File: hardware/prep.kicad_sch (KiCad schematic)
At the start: 20 parts, among them U1 LD1117S33TR_SOT223, U2 LM4040DBZ-10

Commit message: Corrected resistor package, deleted unused files and gerbers
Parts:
- FB1, FB2, FB3, FB4: LCSC (none) -> C73326
- R1: footprint Resistor_SMD:R_4020_10251Metric -> Resistor_SMD:R_0402_1005Metric
- U1: LCSC (none) -> C86781
- U2: LCSC (none) -> C3717582
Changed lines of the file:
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@@
+			)
+		)
+		(property "LCSC" "C3717582"
+			(at 198.12 119.38 0)
+			(effects
+				(font
+					(size 1.27 1.27)
+				)
+				(hide yes)
 			)
 		)
@@
 			)
 		)
+		(property "LCSC" "C73326"
+			(at 115.57 127 90)
+			(effects
+				(font
+					(size 1.27 1.27)
+				)
+				(hide yes)
+			)
+		)
 		(pin "1"
 		)
@@
 			)
 		)
+		(property "LCSC" ""
+			(at 93.98 82.55 0)
+			(effects
+				(font
+					(size 1.27 1.27)
+				)
+				(hide yes)
+			)
+		)
 		(pin "2"
 		)
@@
 			)
 		)
+		(property "LCSC" "C73326"
+			(at 73.66 69.85 90)
+			(effects
+				(font
+					(size 1.27 1.27)
+				)
+				(hide yes)
+			)
+		)
 		(pin "1"
 		)
@@
 			)
 		)
+		(property "LCSC" "C73326"
+			(at 73.66 54.61 90)
+			(effects
+				(font
+					(size 1.27 1.27)
+				)
+				(hide yes)
+			)
+		)
 		(pin "1"
 		)
@@
 			)
 		)
+		(property "LCSC" "C73326"
+			(at 73.66 38.1 90)
+			(effects
+				(font
+					(size 1.27 1.27)
+				)
+				(hide yes)
+			)
+		)
 		(pin "1"
 		)
@@
 			)
 		)
+		(property "LCSC" "C86781"
+			(at 78.74 127 0)
+			(effects
+				(font
+					(size 1.27 1.27)
+				)
+				(hide yes)
+			)
+		)
 		(pin "3"
 		)
@@
 			)
 		)
-		(property "Footprint" "Resistor_SMD:R_4020_10251Metric"
+		(property "Footprint" "Resistor_SMD:R_0402_1005Metric"
 			(at 186.69 119.38 0)
 			(effects

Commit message: bom generation
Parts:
- C1, C10, C2, C3, C4, C5, C6, C7: LCSC (none) -> C45783
- C8: LCSC (none) -> C7411876
- C9: value 22uF -> 100nF; LCSC (none) -> C7411876
- D1, D2, D3: LCSC (none) -> C552852
- R1: LCSC (none) -> C6549338
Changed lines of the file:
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@@
+			)
+		)
+		(property "LCSC" "C45783"
+			(at 102.87 82.55 0)
+			(effects
+				(font
+					(size 1.27 1.27)
+				)
+				(hide yes)
 			)
 		)
@@
 			)
 		)
+		(property "LCSC" "C45783"
+			(at 121.92 82.55 0)
+			(effects
+				(font
+					(size 1.27 1.27)
+				)
+				(hide yes)
+			)
+		)
 		(pin "2"
 		)
@@
 			)
 		)
-		(property "LCSC" ""
+		(property "LCSC" "C45783"
 			(at 93.98 82.55 0)
 			(effects
@@
 			)
 		)
+		(property "LCSC" "C7411876"
+			(at 91.44 144.78 0)
+			(effects
+				(font
+					(size 1.27 1.27)
+				)
+				(hide yes)
+			)
+		)
 		(pin "2"
 		)
@@
 			)
 		)
+		(property "LCSC" "C45783"
+			(at 64.77 144.78 0)
+			(effects
+				(font
+					(size 1.27 1.27)
+				)
+				(hide yes)
+			)
+		)
 		(pin "2"
 		)
@@
 			)
 		)
+		(property "LCSC" "C45783"
+			(at 113.03 82.55 0)
+			(effects
+				(font
+					(size 1.27 1.27)
+				)
+				(hide yes)
+			)
+		)
 		(pin "2"
 		)
@@
 			)
 		)
+		(property "LCSC" "C552852"
+			(at 86.36 69.85 0)
+			(effects
+				(font
+					(size 1.27 1.27)
+				)
+				(hide yes)
+			)
+		)
 		(pin "1"
 		)
@@
 			)
 		)
+		(property "LCSC" "C45783"
+			(at 139.7 82.55 0)
+			(effects
+				(font
+					(size 1.27 1.27)
+				)
+				(hide yes)
+			)
+		)
 		(pin "2"
 		)
@@
 			)
 		)
-		(property "Value" "22uF"
+		(property "Value" "100nF"
 			(at 106.68 146.0562 0)
 			(effects
@@
 			)
 		)
+		(property "LCSC" "C7411876"
+			(at 104.14 144.78 0)
+			(effects
+				(font
+					(size 1.27 1.27)
+				)
+				(hide yes)
+			)
+		)
 		(pin "2"
 		)
@@
 			)
 		)
+		(property "LCSC" "C45783"
+			(at 198.12 132.08 90)
+			(effects
+				(font
+					(size 1.27 1.27)
+				)
+				(hide yes)
+			)
+		)
 		(pin "2"
 		)
@@
 			)
 		)
+		(property "LCSC" "C552852"
+			(at 86.36 54.61 0)
+			(effects
+				(font
+					(size 1.27 1.27)
+				)
+				(hide yes)
+			)
+		)
 		(pin "1"
 		)
@@
 			)
 		)
+		(property "LCSC" "C6549338"
+			(at 186.69 119.38 90)
+			(effects
+				(font
+					(size 1.27 1.27)
+				)
+				(hide yes)
+			)
+		)
 		(pin "1"
 		)
@@
 			)
 		)
+		(property "LCSC" "C45783"
+			(at 130.81 82.55 0)
+			(effects
+				(font
+					(size 1.27 1.27)
+				)
+				(hide yes)
+			)
+		)
 		(pin "2"
 		)
@@
 			(at 86.36 38.1 0)
 			(effects
+				(font
+					(size 1.27 1.27)
+				)
+				(hide yes)
+			)
+		)
+		(property "LCSC" "C552852"
+			(at 86.36 38.1 0)
+			(effects

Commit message: fix 10uF cap part ref
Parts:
- C8: LCSC C7411876 -> C17314042
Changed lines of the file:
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@@
 			)
 		)
-		(property "LCSC" "C7411876"
+		(property "LCSC" "C17314042"
 			(at 91.44 144.78 0)
 			(effects

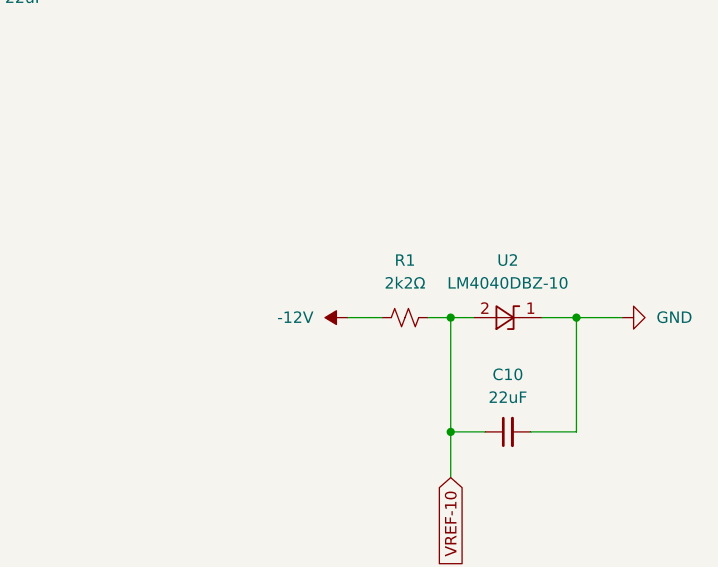
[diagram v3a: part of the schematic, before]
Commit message: Removed ohm symbol to not break JCLPCB BOM
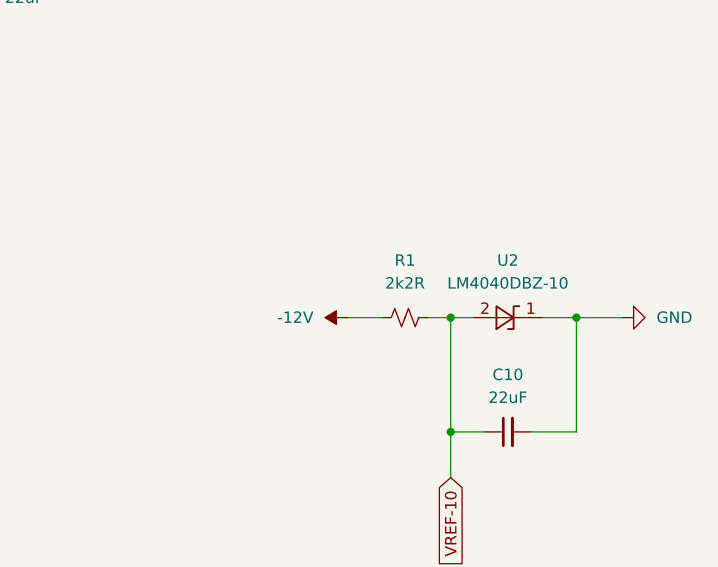
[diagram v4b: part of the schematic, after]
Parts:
- R1: value 2k2Ω -> 2k2R
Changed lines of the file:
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@@
 			)
 		)
-		(property "Value" "2k2Ω"
+		(property "Value" "2k2R"
 			(at 186.69 115.57 90)
 			(effects
